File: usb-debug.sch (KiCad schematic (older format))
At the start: 77 parts, among them IC15 TPS7A0518PDBVT, IC16 AP22652W6-7, IC7 HD3SS3220, J11 632723300011, Q1 PMV32UP, T6 BSS138APW, T7 BSS138APW

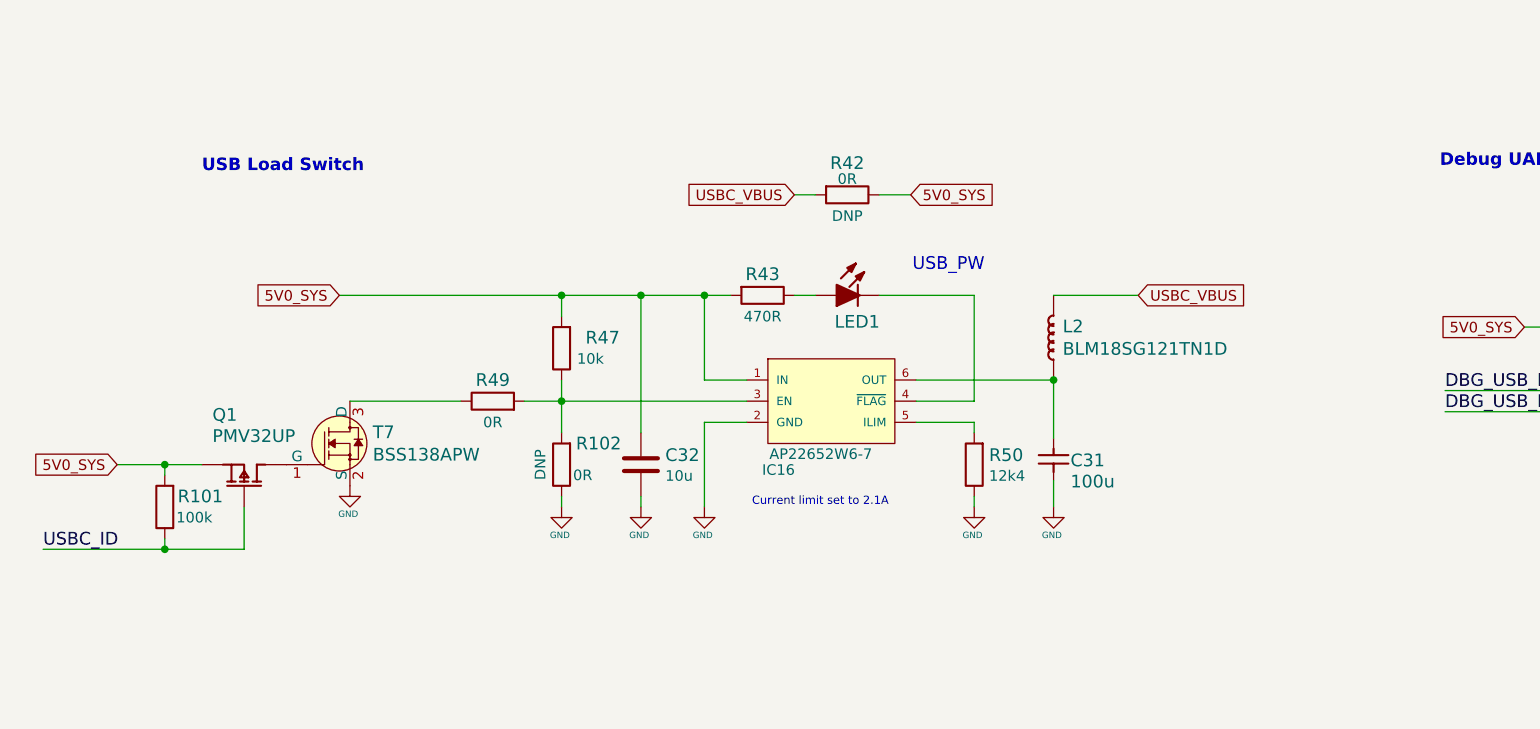
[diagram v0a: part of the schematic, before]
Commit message: Add T7 pull-down
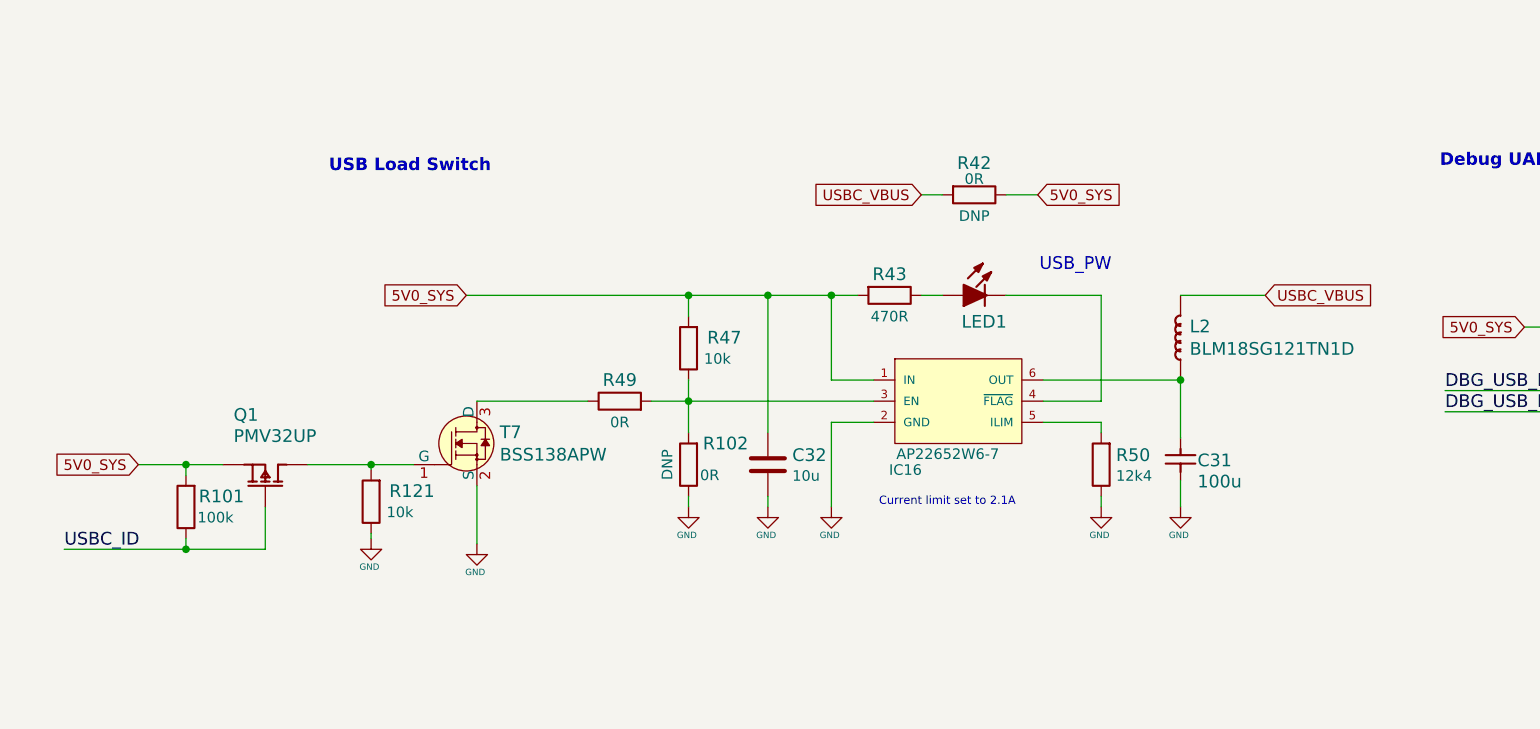
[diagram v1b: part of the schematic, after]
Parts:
- added R121: R_10k_0402, jetson-nano-baseboard-footprints:0402-res, symbol jetson-nano-baseboard:R_10k_0402
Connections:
- net GND: now also R121.1
- net at Q1.3 (D), T7.1 (G): now also R121.2
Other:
- moved on the sheet: C31, C32, IC16, L2, LED1, Q1, R101, R102, R42, R43, R47, R49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

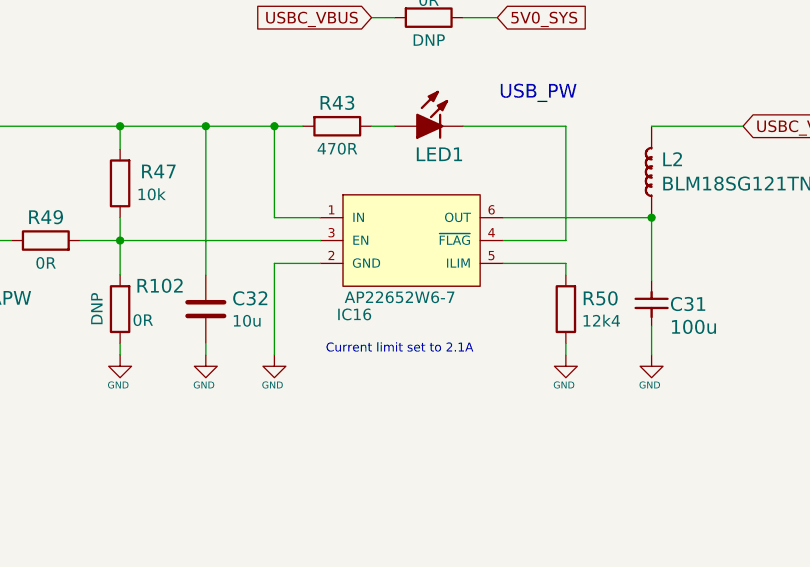
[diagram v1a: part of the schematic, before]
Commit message: Replace AP22652AW6-7 with AP22653W6-7
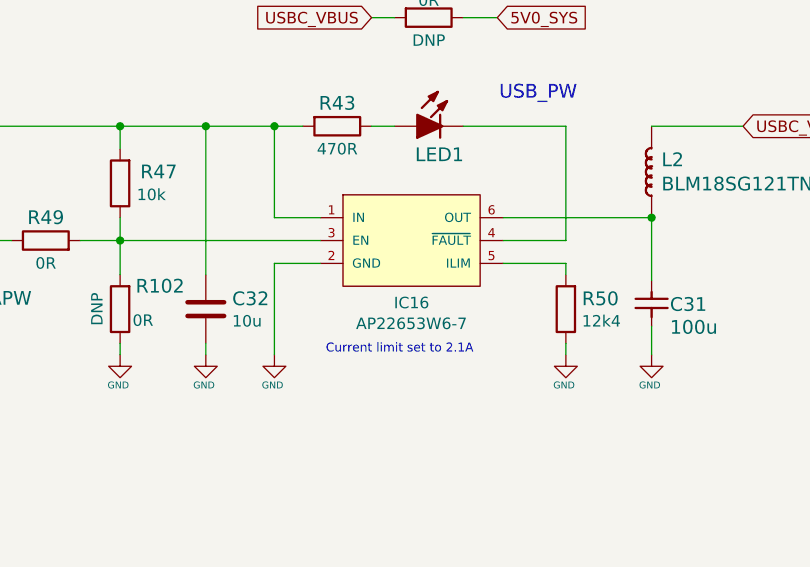
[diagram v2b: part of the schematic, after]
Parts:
- removed IC16: AP22652W6-7, jetson-nano-baseboard-footprints:SOT-23-6, symbol jetson-nano-baseboard:AP22652W6-7
- added IC16: AP22653W6-7, jetson-nano-baseboard-footprints:SOT-23-6, symbol jetson-nano-baseboard:AP22653W6-7
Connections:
- net 5V0_SYS: now also IC16.1 (IN)
- net GND: now also IC16.2 (GND)
- net at C31.2, L2.1 (P): now also IC16.6 (OUT)
- net at LED1.K: now also IC16.4 (~FAULT~)
- net at R102.2, R47.1, R49.2: now also IC16.3 (EN)
- net at R50.2: now also IC16.5 (ILIM)
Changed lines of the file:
@@
-	1    0    0    -1
-$EndComp
-$Comp
-L jetson-nano-baseboard:AP22652W6-7 IC16
-U 1 1 618DCEF2
-P 4925 9475
-F 0 "IC16" H 4675 9150 50  0000 C CNN
-F 1 "AP22652W6-7" H 4875 9225 50  0000 C CNN
-F 2 "jetson-nano-baseboard-footprints:SOT-23-6" H 4925 9225 50  0001 C CNN
-F 3 "https://www.diodes.com/assets/Datasheets/AP22652_53_52A_53A.pdf" H 4925 9475 50  0001 C CNN
-F 4 "Diodes Incorporated " H 4925 9125 50  0001 C CNN "Manufacturer"
-F 5 "" H 4925 9475 50  0000 C CNN "DNP"
-	1    4925 9475
 	1    0    0    -1
 $EndComp
@@
 Wire Wire Line
 	2650 9875 2650 10150
+$Comp
+L jetson-nano-baseboard:AP22653W6-7 IC16
+U 1 1 62637B7A
+P 4925 9475
+F 0 "IC16" H 4925 9202 50  0000 C CNN
+F 1 "AP22653W6-7" H 4925 9111 50  0000 C CNN
+F 2 "jetson-nano-baseboard-footprints:SOT-23-6" H 4925 9225 50  0001 C CNN
+F 3 "https://www.diodes.com/assets/Datasheets/AP22652_53_52A_53A.pdf" H 4925 9475 50  0001 C CNN
+F 4 "Diodes Incorporated " H 4925 9125 50  0001 C CNN "Manufacturer"
+F 5 "AP22653W6-7" H 4925 9475 50  0001 C CNN "MPN"
+	1    4925 9475
+	1    0    0    -1
+$EndComp
 $EndSCHEMATC
